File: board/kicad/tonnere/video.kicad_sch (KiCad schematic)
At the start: 29 parts, among them J4 HDMI_A, J6 DE15_Pins_HighDensity_Mountin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, U1 TPD4E02B04DQA, U11 TPD4E02B04DQA, U2 TPD4E02B04DQA, U21 THS7316DR, U3 TPD4E02B04DQA

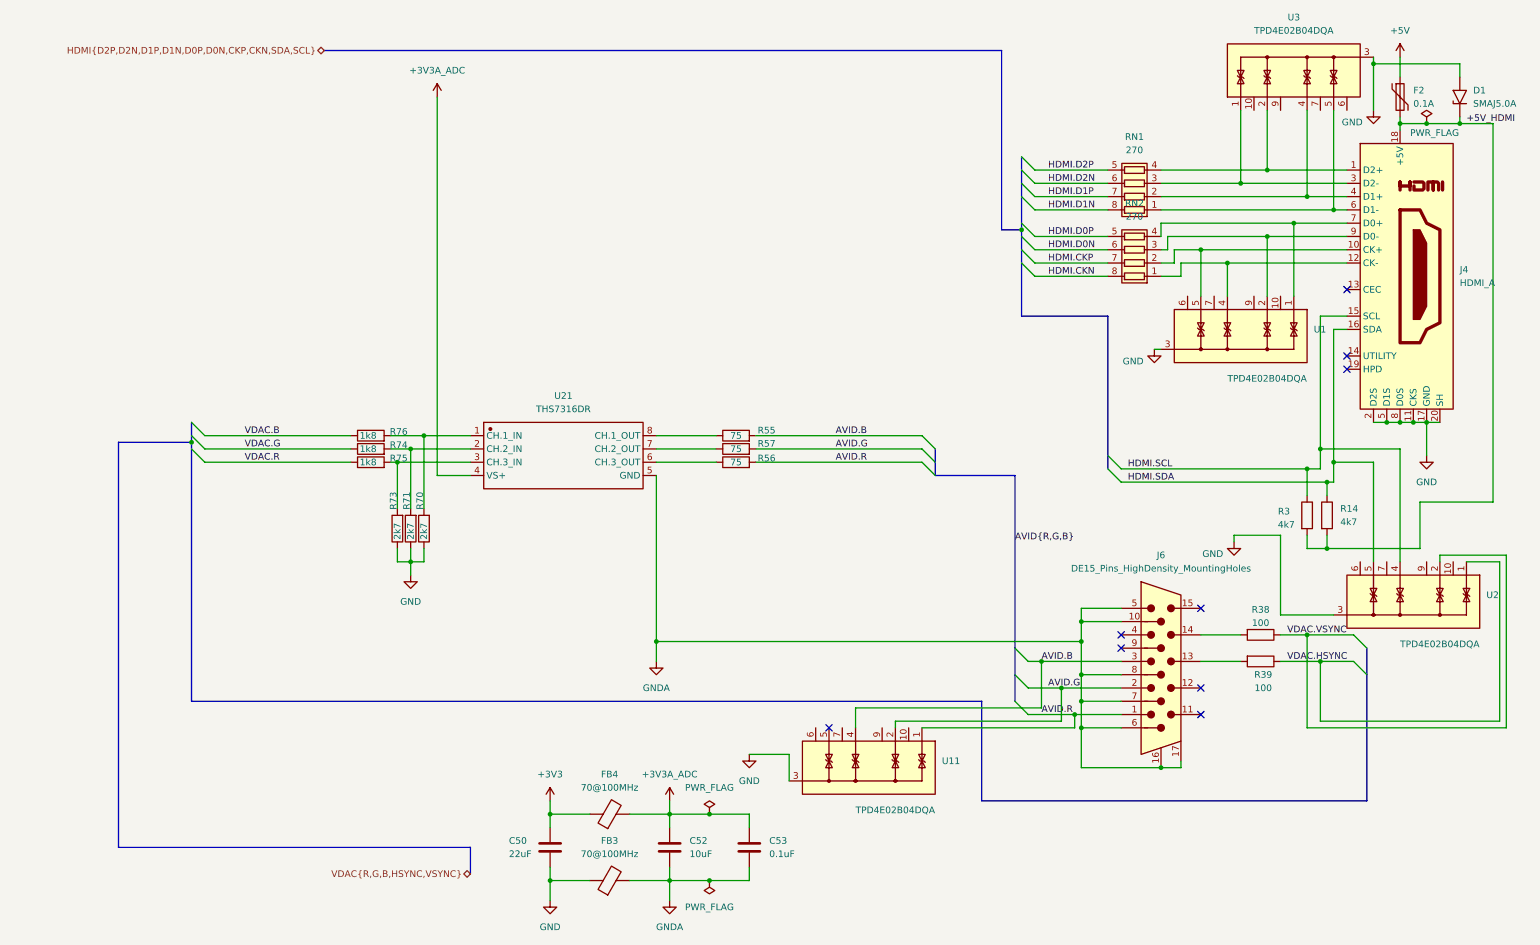
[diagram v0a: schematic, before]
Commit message: 0.60 (not final). Fix errata from 0.51. Added USB2 phy.
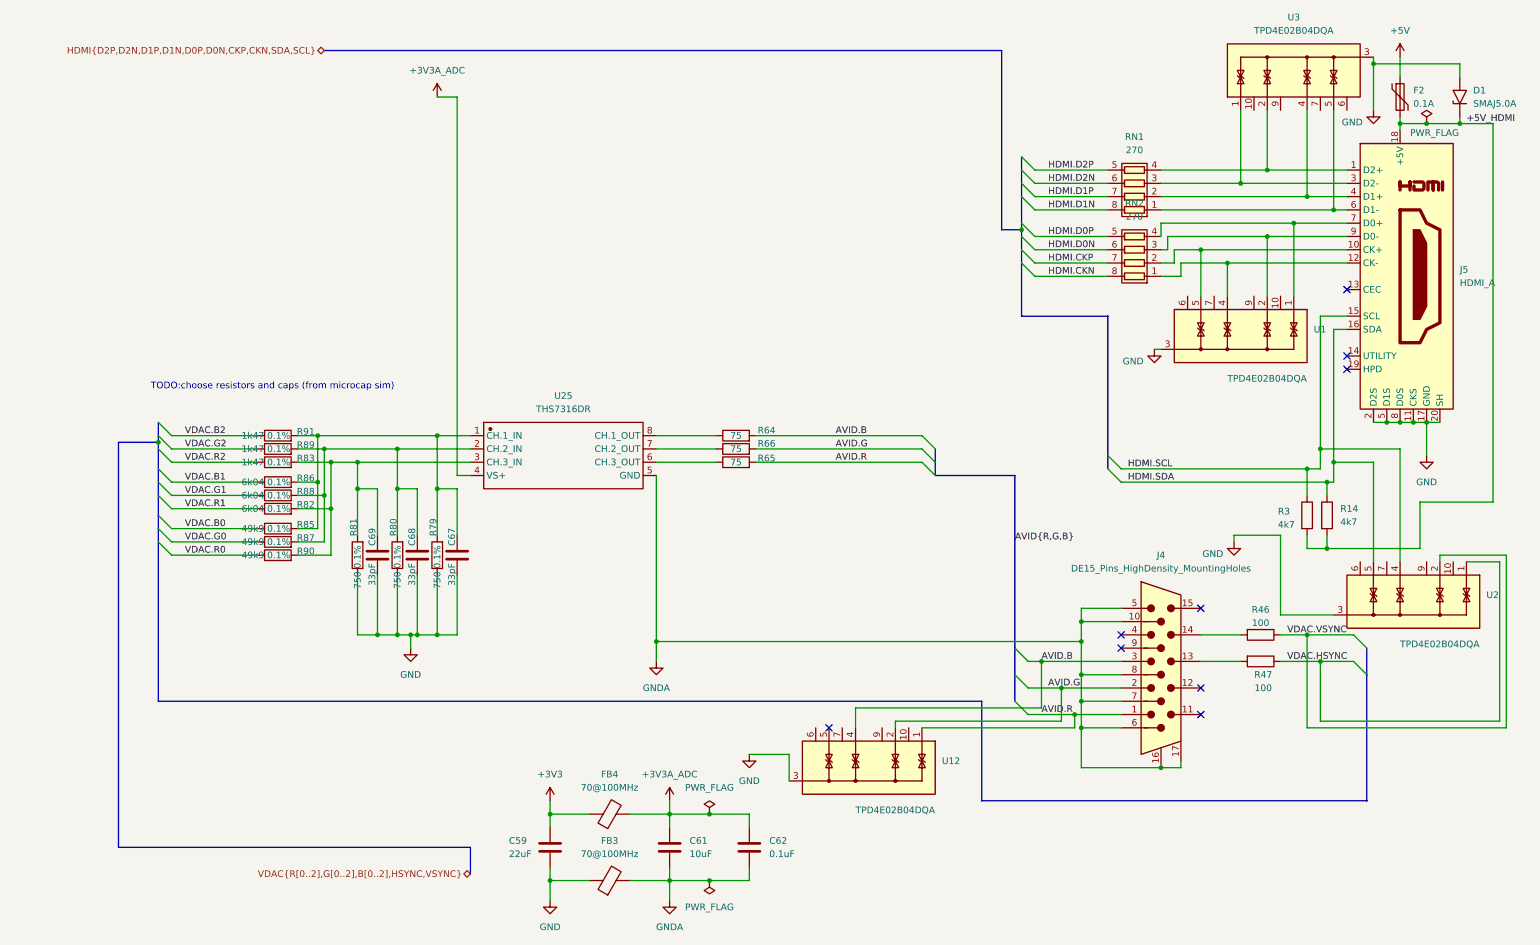
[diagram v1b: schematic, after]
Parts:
- added C67, C68, C69: 33pF, Capacitor_SMD:C_0603_1608Metric, symbol Device:C
- added R82, R86, R88: 6k04 0.1%, Resistor_SMD:R_0603_1608Metric, symbol Device:R
- added R85, R87, R90: 49k9 0.1%, Resistor_SMD:R_0603_1608Metric, symbol Device:R
- J4: renamed from J6; JLC_3DModel (none) -> 3aa2d893d3fe4a0a80cdfd9bf1095edb; JLC_3D_Size (none) -> 30.805 14.801
- R79: renamed from R70; value 2k7 -> 750 0.1%
- R80: renamed from R71; value 2k7 -> 750 0.1%
- R81: renamed from R73; value 2k7 -> 750 0.1%
- R83: renamed from R75; value 1k8 -> 1k47 0.1%
- R89: renamed from R74; value 1k8 -> 1k47 0.1%
- R91: renamed from R76; value 1k8 -> 1k47 0.1%
- renumbered C50 to C59, C52 to C61, C53 to C62, J4 to J5, R38 to R46, R39 to R47, R55 to R64, R56 to R65, R57 to R66, U11 to U12, U21 to U25
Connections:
- net GND: now also C67.2, C68.2, C69.2
- net at R80.2, R89.2, U25.2 (CH.2_IN): now also C68.1, R87.2, R88.2
- net at R81.2, R83.2, U25.3 (CH.3_IN): now also C69.1, R82.2, R90.2
- net at R79.2, R91.2, U25.1 (CH.1_IN): now also C67.1, R85.2, R86.2
- net VDAC.B renamed VDAC.B2
- net VDAC.G renamed VDAC.G2
- net VDAC.R renamed VDAC.R2
- new net VDAC.B0: R85.1
- new net VDAC.B1: R86.1
- new net VDAC.G0: R87.1
- new net VDAC.G1: R88.1
- new net VDAC.R0: R90.1
- new net VDAC.R1: R82.1
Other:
- note added: "TODO:choose resistors and caps (from microcap sim)"
- moved on the sheet: R79, R80, R81, R83, R89, R91
